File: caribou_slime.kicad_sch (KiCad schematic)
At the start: 2 parts, among them U1 ESP32-C3_SUPERMINI, U2 BMI270

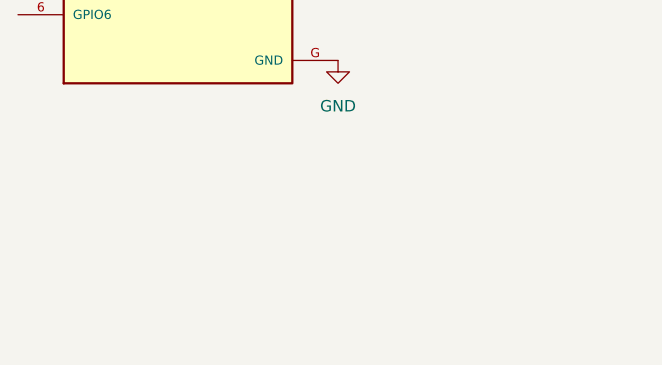
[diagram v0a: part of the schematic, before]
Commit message: Make TP4056 charging board eCAD files
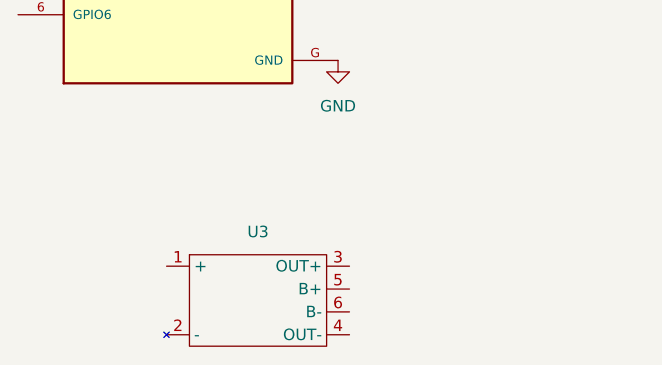
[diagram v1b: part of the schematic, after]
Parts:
- added U3: ~, TP4056_Charging_Board:TP4056 Charging Board, symbol TP4056_Board:TP4056
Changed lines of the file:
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@@
 (kicad_sch (version 20230121) (generator eeschema)
   (paper "A4")
+  (symbol (lib_id "TP4056_Board:TP4056") (at 72.39 106.68 0) (unit 1)
+    (in_bom yes) (on_board yes) (dnp no) (fields_autoplaced)
+    (property "Reference" "U3" (at 72.39 92.71 0)
+      (effects (font (size 1.27 1.27)))
+    )
+    (property "Value" "~" (at 72.39 106.68 0)
+      (effects (font (size 1.27 1.27)))
+    )
+    (property "Footprint" "TP4056_Charging_Board:TP4056 Charging Board" (at 72.39 106.68 0)
+      (effects (font (size 1.27 1.27)) hide)
+    )
+    (property "Datasheet" "" (at 72.39 106.68 0)
+      (effects (font (size 1.27 1.27)) hide)
+    )
+    (pin "3")
+    (pin "2")
+    (pin "1")
+    (pin "5")
+    (pin "6")
+    (pin "4")
+    (instances
+      (project "caribou_slime"
+        (path "/61bfc64c-87c3-434a-8ade-1f9e7b05e459"
+          (reference "U3") (unit 1)
+        )
+      )
+    )
+  )
   (symbol (lib_id "BMI270:BMI270") (at 153.67 60.96 0) (unit 1)
     (in_bom yes) (on_board yes) (dnp no) (fields_autoplaced)

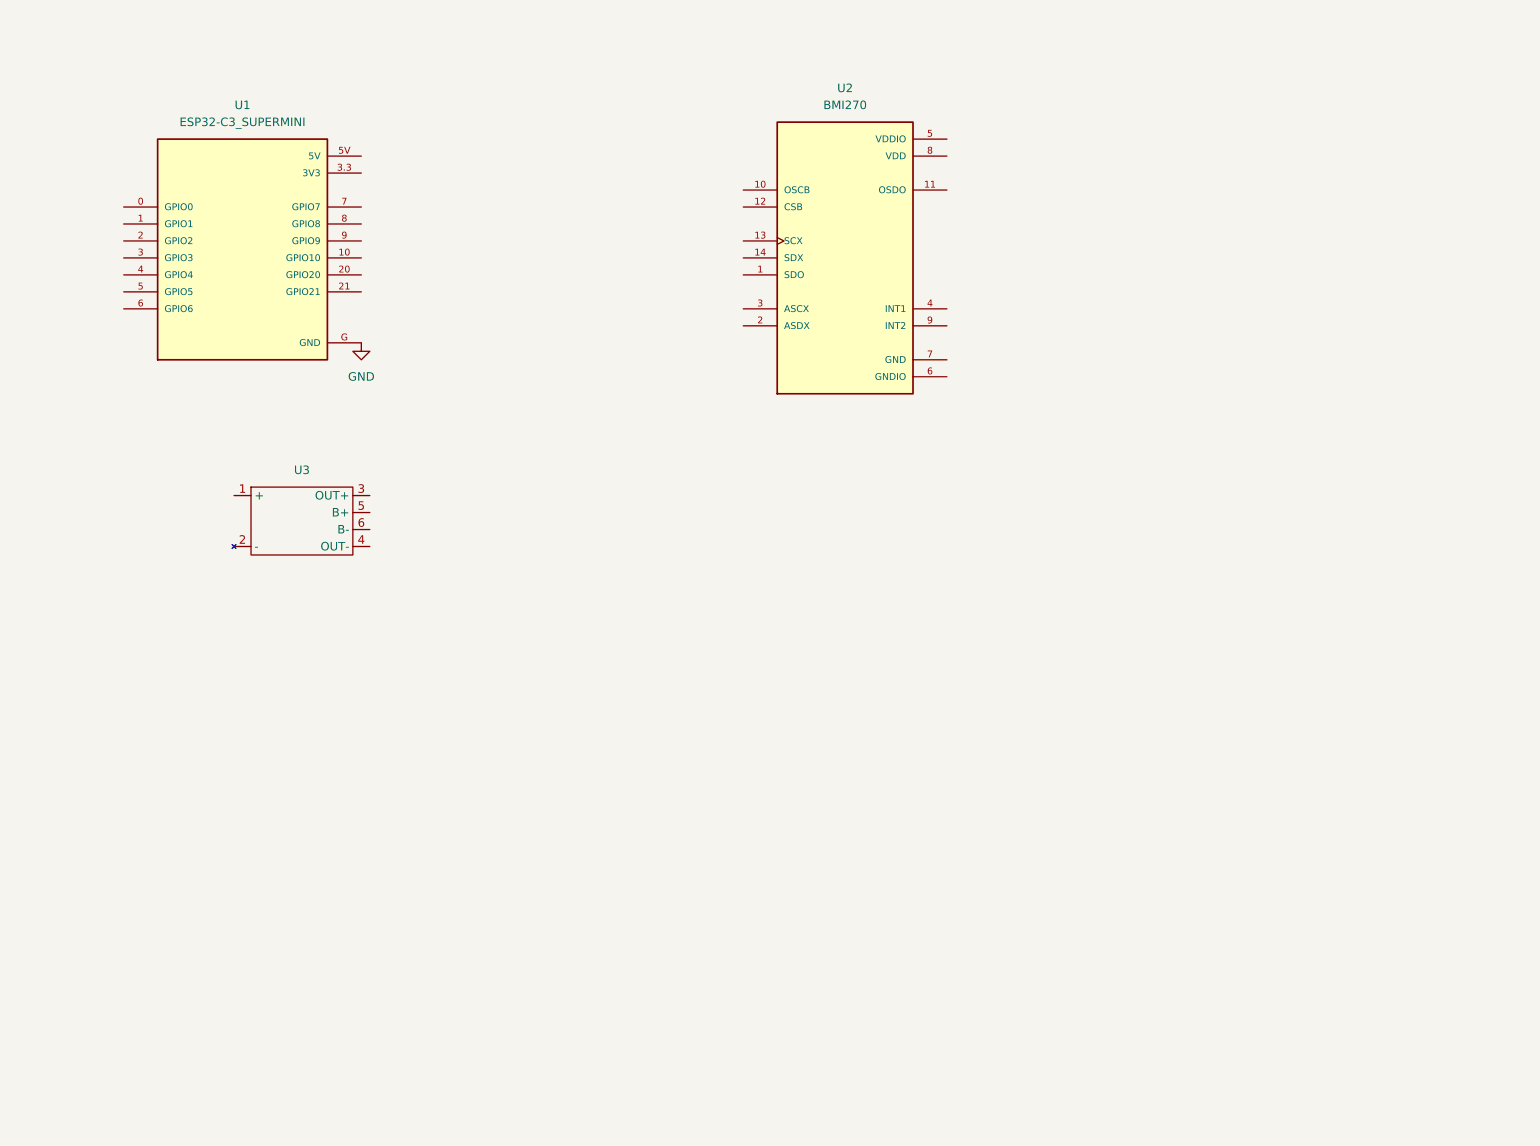
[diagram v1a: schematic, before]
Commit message: Add BMI 270 circuit to schematic
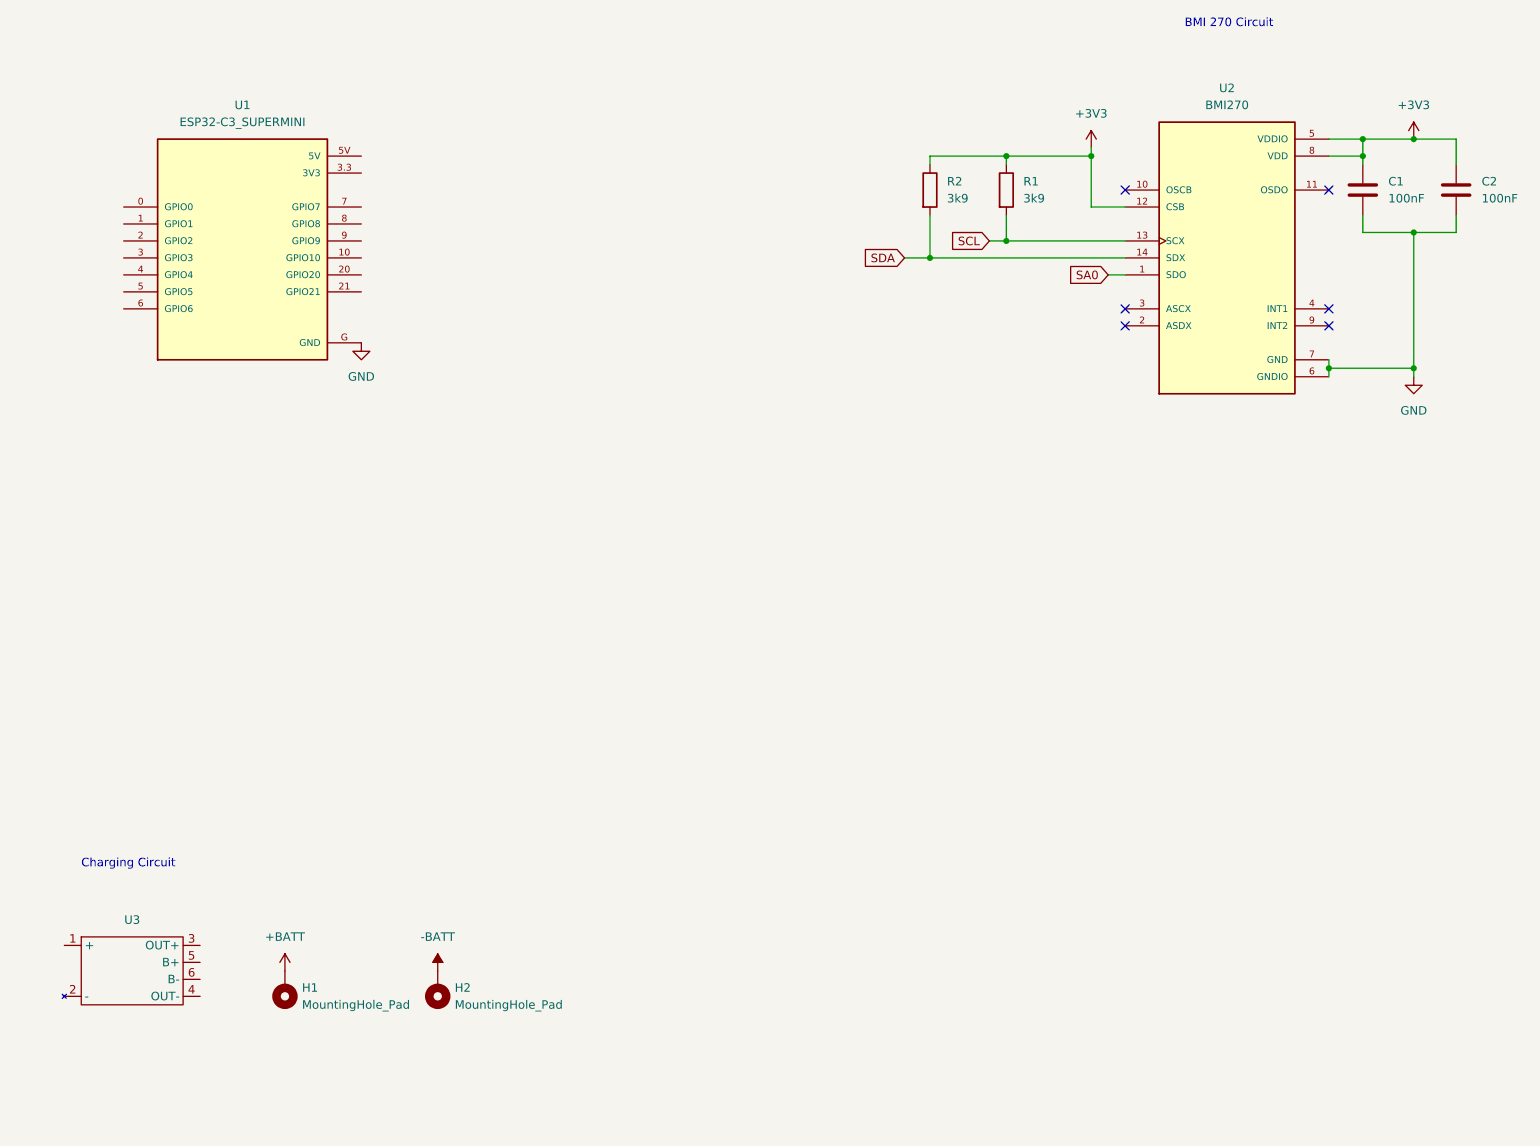
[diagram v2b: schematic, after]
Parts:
- added C1, C2: 100nF, symbol Device:C
- added H1, H2: MountingHole_Pad, symbol Mechanical:MountingHole_Pad
- added R1, R2: 3k9, symbol Device:R
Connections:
- net GND: now also U2.6 (GNDIO), U2.7 (GND), C1.2, C2.2
- net SA0: now reaches U2.1 (SDO)
- net +3V3: now reaches U2.12 (CSB)
- net +3V3: now also U2.5 (VDDIO), U2.8 (VDD), C1.1, C2.1, R1.1, R2.1
- net SCL: now reaches U2.13 (SCX)
- net SCL: now also R1.2
- net SDA: now reaches U2.14 (SDX)
- net SDA: now also R2.2
- new net +BATT: H1.1
- new net -BATT: H2.1
- no-connect marks 0 -> 6
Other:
- note added: "BMI 270 Circuit"
- note added: "Charging Circuit"
- moved on the sheet: U2, U3

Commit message: Add ucontroller circuit to schematic
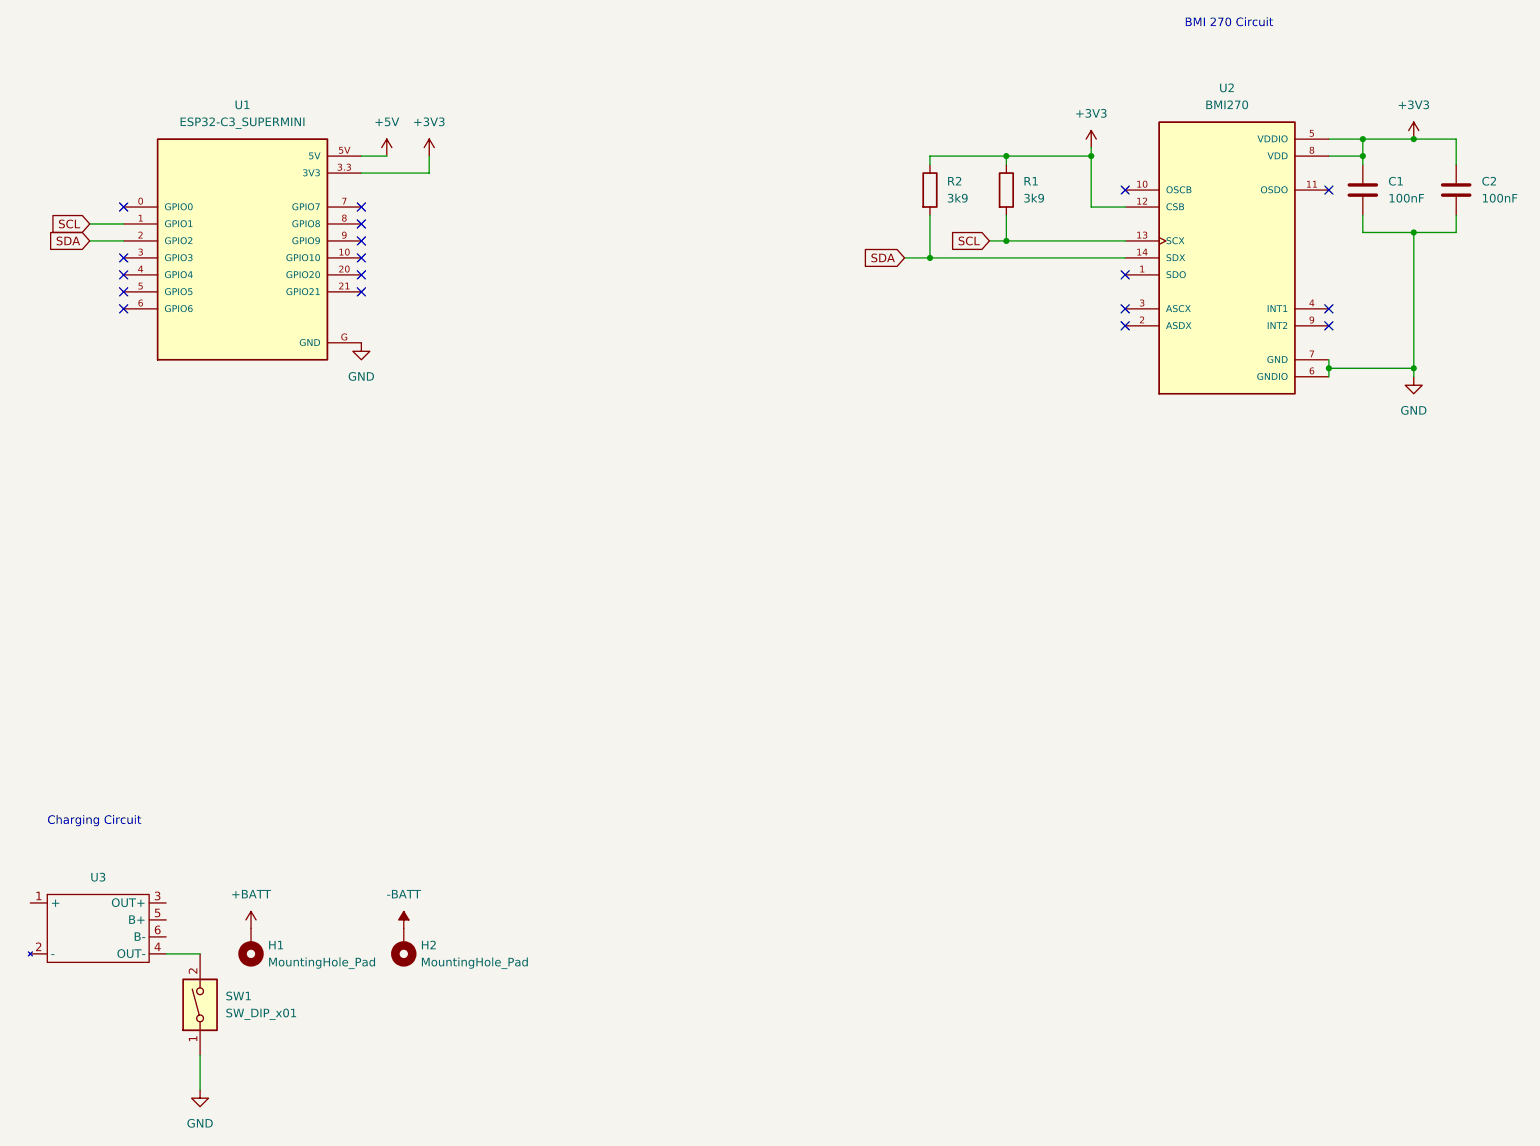
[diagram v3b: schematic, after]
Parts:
- added SW1: SW_DIP_x01, symbol Switch:SW_DIP_x01
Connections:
- net +3V3: now also U1.3.3 (3V3)
- net GND: now also SW1.1
- net SCL: now also U1.1 (GPIO1)
- net SDA: now also U1.2 (GPIO2)
- net at U3.4 (OUT-): now also SW1.2
- net +5V: now reaches U1.5V
- net SA0: no longer names the net of U2.1 (SDO)
- no-connect marks 6 -> 18
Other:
- moved on the sheet: H1, H2, U3

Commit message: Add TP4056 circuit to schematic
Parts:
- added D1, D2: 1N5817, Diode_THT:D_DO-41_SOD81_P10.16mm_Horizontal, symbol Diode:1N5817
- H1: value MountingHole_Pad -> B+
- H2: value MountingHole_Pad -> B-
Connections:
- net +BATT is gone; now on an unnamed net: H1.1
- net -BATT is gone; now on an unnamed net: H2.1
- net +5V: now also D1.1 (K), D2.1 (K)
- net at U3.1 (+): now also D1.2 (A)
- net at U3.3 (OUT+): now also D2.2 (A)
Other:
- moved on the sheet: H1, H2, SW1, U3
